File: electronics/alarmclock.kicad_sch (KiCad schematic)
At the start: 31 parts, among them J1 Conn_01x02, J2 SWD, J3 SocketTop, J4 SocketBottom, J5 Conn_01x02, Q1 Backpower, SW1 Rotary_Encoder_Switch, SW2 Reset, U1 STM32L031F6P6, U2 74HC595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

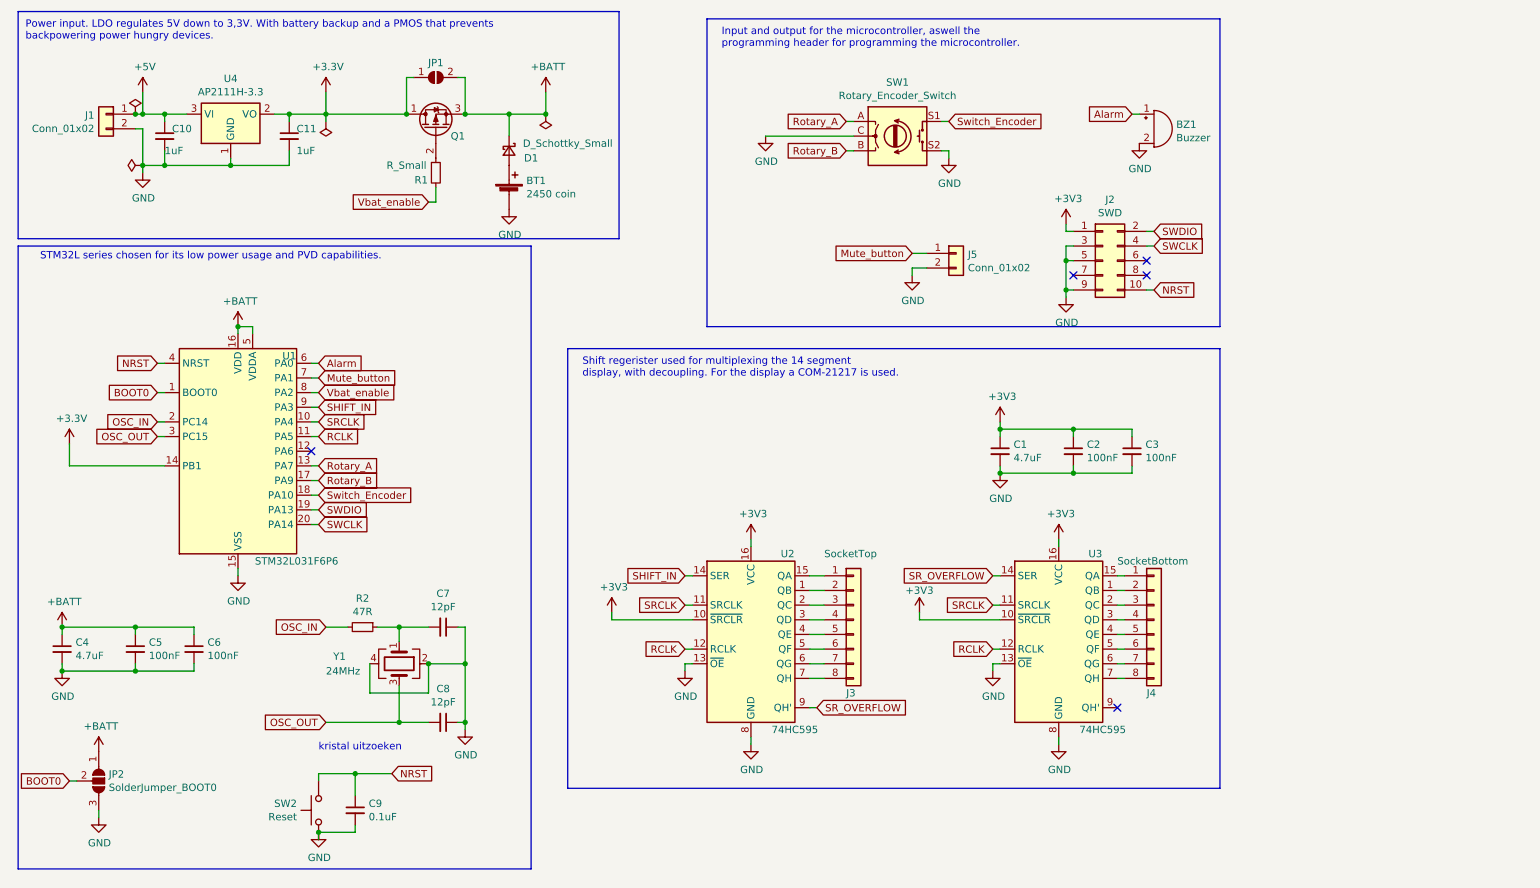
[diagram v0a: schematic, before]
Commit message: added currentlimiting resistors
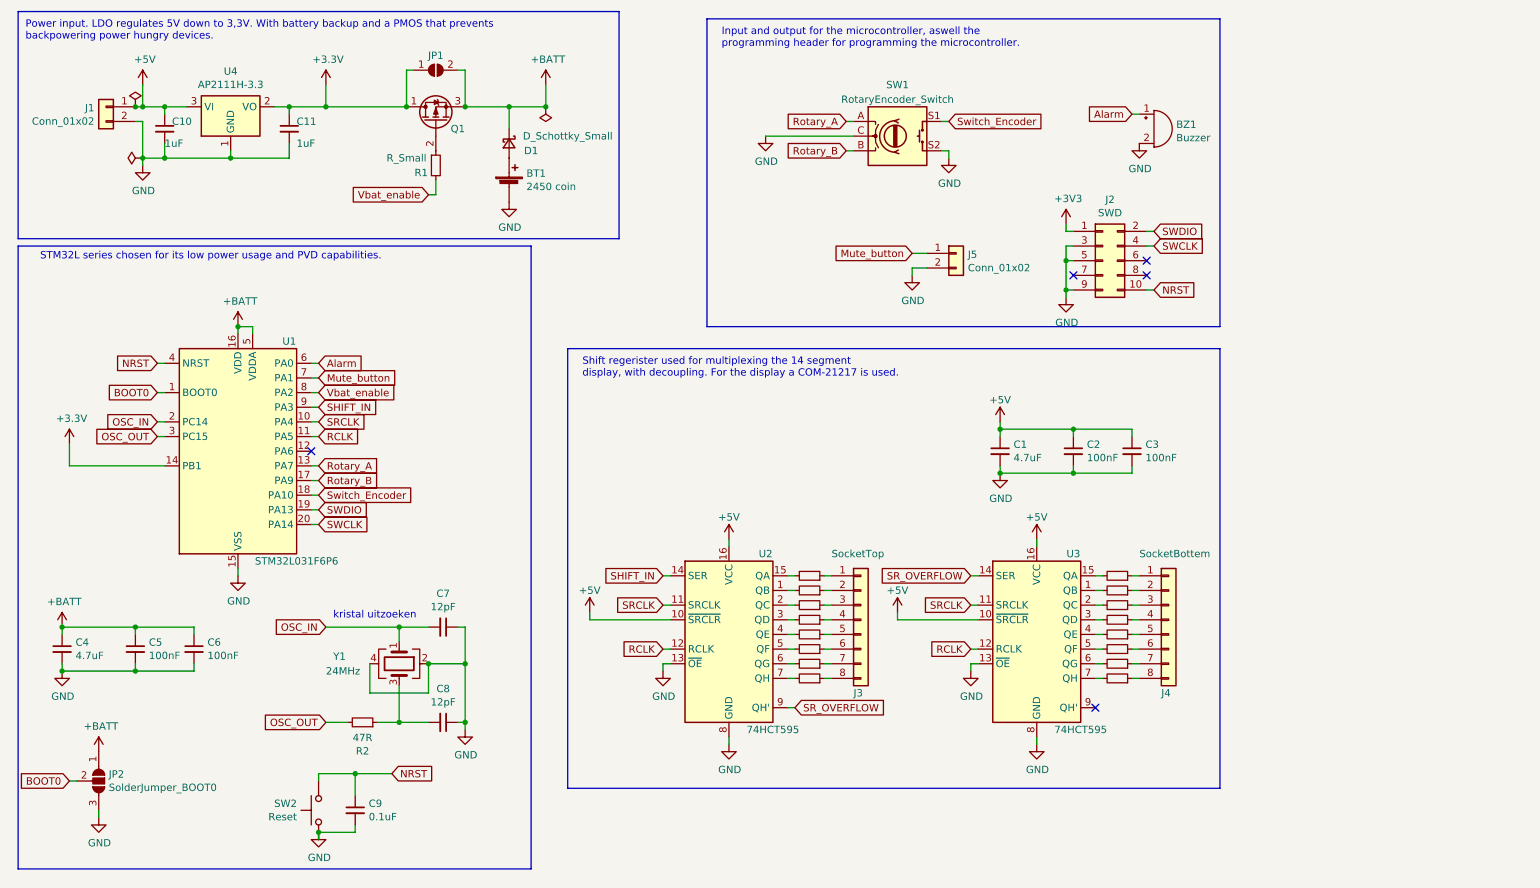
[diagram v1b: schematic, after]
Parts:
- removed SW1: Rotary_Encoder_Switch, Connector_PinHeader_2.54mm:PinHeader_1x05_P2.54mm_Vertical, symbol Device:Rotary_Encoder_Switch
- added R10, R11, R12, R13, R14, R15, R16, R17, R18, R3, R4, R5, R6, R7, R8, R9: R_Small, symbol Device:R_Small
- added SW1: RotaryEncoder_Switch, symbol Device:RotaryEncoder_Switch
- J4: value SocketBottom -> SocketBottem
- U2, U3: value 74HC595 -> 74HCT595
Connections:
- net +3V3: no longer C1.1, C2.1, C3.1, U2.10 (~{SRCLR}), U2.16 (VCC), U3.10 (~{SRCLR}), U3.16 (VCC)
- net +5V: now also C1.1, C2.1, C3.1, U2.10 (~{SRCLR}), U2.16 (VCC), U3.10 (~{SRCLR}), U3.16 (VCC)
- net GND: now also SW1.C, SW1.S2
- net OSC_IN: now also C7.2, Y1.1; no longer R2.2
- net OSC_OUT: now also R2.2; no longer C8.2, Y1.3
- net Rotary_A: now also SW1.A
- net Rotary_B: now also SW1.B
- net Switch_Encoder: now also SW1.S1
- net at U3.15 (QA): now also R9.2; no longer J4.1 (Pin_1)
- net at U3.1 (QB): now also R12.2; no longer J4.2 (Pin_2)
- net at U3.2 (QC): now also R13.2; no longer J4.3 (Pin_3)
- net at U3.3 (QD): now also R14.2; no longer J4.4 (Pin_4)
- net at U3.4 (QE): now also R15.2; no longer J4.5 (Pin_5)
- net at U3.5 (QF): now also R16.2; no longer J4.6 (Pin_6)
- net at U3.6 (QG): now also R17.2; no longer J4.7 (Pin_7)
- net at U3.7 (QH): now also R18.2; no longer J4.8 (Pin_8)
- net at J3.1 (Pin_1): now also R3.1; no longer U2.15 (QA)
- net at J3.2 (Pin_2): now also R4.1; no longer U2.1 (QB)
- net at J3.3 (Pin_3): now also R5.1; no longer U2.2 (QC)
- net at J3.4 (Pin_4): now also R6.1; no longer U2.3 (QD)
- net at J3.5 (Pin_5): now also R7.1; no longer U2.4 (QE)
- net at J3.6 (Pin_6): now also R8.1; no longer U2.5 (QF)
- net at J3.7 (Pin_7): now also R10.1; no longer U2.6 (QG)
- net at J3.8 (Pin_8): now also R11.1; no longer U2.7 (QH)
- new net: C8.2, R2.1, Y1.3
- new net: R4.2, U2.1 (QB)
- new net: R3.2, U2.15 (QA)
- new net: R5.2, U2.2 (QC)
- new net: R6.2, U2.3 (QD)
- new net: R7.2, U2.4 (QE)
- new net: R8.2, U2.5 (QF)
- new net: R10.2, U2.6 (QG)
- new net: R11.2, U2.7 (QH)
- new net: J4.2 (Pin_2), R12.1
- new net: J4.1 (Pin_1), R9.1
- new net: J4.3 (Pin_3), R13.1
- new net: J4.4 (Pin_4), R14.1
- new net: J4.5 (Pin_5), R15.1
- new net: J4.6 (Pin_6), R16.1
- new net: J4.7 (Pin_7), R17.1
- new net: J4.8 (Pin_8), R18.1
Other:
- moved on the sheet: BT1, C10, C11, D1, J1, J3, JP1, Q1, R1, R2, U2, U3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

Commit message: made most of the pcb
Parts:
- removed R13, R14, R15, R16, R5, R6, R7: R_Small, symbol Device:R_Small
- removed R2: 47R, Resistor_SMD:R_1206_3216Metric, symbol Device:R_Small
- added J6, J7: Conn_01x05, Connector_PinHeader_2.54mm:PinHeader_1x05_P2.54mm_Vertical, symbol Connector_Generic:Conn_01x05
- C7, C8: footprint Capacitor_SMD:C_1206_3216Metric -> Capacitor_SMD:C_0805_2012Metric
- D1: footprint (none) -> Diode_SMD:D_1206_3216Metric_Pad1.42x1.75mm_HandSolder
- J1, J5: footprint (none) -> Connector_PinHeader_2.54mm:PinHeader_1x02_P2.54mm_Vertical
- JP1: footprint (none) -> Jumper:SolderJumper-2_P1.3mm_Open_TrianglePad1.0x1.5mm
- JP2: footprint (none) -> Jumper:SolderJumper-3_P2.0mm_Open_TrianglePad1.0x1.5mm
- Q1: footprint (none) -> Package_TO_SOT_SMD:SOT-323_SC-70_Handsoldering
- R1, R10, R11, R12, R17, R18, R3, R4, R8, R9: footprint (none) -> Resistor_SMD:R_1206_3216Metric
- SW1: footprint (none) -> Rotary_Encoder:RotaryEncoder_Bourns_Horizontal_PEC09-2xxxF-Nxxxx
- U2, U3: footprint (none) -> Package_SO:TSSOP-16_4.4x5mm_P0.65mm
- Y1: footprint (none) -> Crystal:Crystal_SMD_SeikoEpson_MC146-4Pin_6.7x1.5mm_HandSoldering
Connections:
- net +5V: now also J1.2 (Pin_2), J6.5 (Pin_5), J7.5 (Pin_5); no longer J1.1 (Pin_1)
- net Alarm: now also BZ1.2 (+); no longer BZ1.1 (-)
- net GND: now also BZ1.1 (-), J1.1 (Pin_1), J5.1 (Pin_1), SW2.1, J6.1 (Pin_1), J7.1 (Pin_1); no longer BZ1.2 (+), J1.2 (Pin_2), J5.2 (Pin_2), SW2.2
- net Mute_button: now also J5.2 (Pin_2); no longer J5.1 (Pin_1)
- net NRST: now also SW2.2; no longer SW2.1
- net OSC_OUT: now also C8.2, Y1.3
- net RCLK: now also U1.9 (PA3), J7.3 (Pin_3); no longer U1.11 (PA5), U2.12 (RCLK), U3.12 (RCLK)
- net Rotary_B: now also U1.11 (PA5); no longer U1.17 (PA9)
- net SHIFT_IN: now also U1.10 (PA4), J7.4 (Pin_4); no longer U1.9 (PA3), U2.14 (SER)
- net SRCLK: now also U1.8 (PA2), J7.2 (Pin_2); no longer U1.10 (PA4), U2.11 (SRCLK), U3.11 (SRCLK)
- net Switch_Encoder: now also U1.12 (PA6); no longer U1.18 (PA10)
- net Vbat_enable: now also U1.17 (PA9); no longer U1.8 (PA2)
- net at J3.3 (Pin_3): now also U2.2 (QC)
- net at J3.4 (Pin_4): now also U2.3 (QD)
- net at J3.5 (Pin_5): now also U2.4 (QE)
- net at U3.2 (QC): now also J4.3 (Pin_3)
- net at U3.3 (QD): now also J4.4 (Pin_4)
- net at U3.4 (QE): now also J4.5 (Pin_5)
- net at U3.5 (QF): now also J4.6 (Pin_6)
- new net RCLK_DIS: J6.3 (Pin_3), U2.12 (RCLK), U3.12 (RCLK)
- new net SHIFT_IN_DIS: J6.4 (Pin_4), U2.14 (SER)
- new net SRCLK_DIS: J6.2 (Pin_2), U2.11 (SRCLK), U3.11 (SRCLK)
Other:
- moved on the sheet: BZ1, C1, C10, C11, C2, C3, J1, J2, J3, J4, J5, SW1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

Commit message: finilised for review
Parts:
- removed SW1: RotaryEncoder_Switch, Rotary_Encoder:RotaryEncoder_Bourns_Horizontal_PEC09-2xxxF-Nxxxx, symbol Device:RotaryEncoder_Switch
- added J8: RotaryEncoder, Connector_PinHeader_2.54mm:PinHeader_1x05_P2.54mm_Vertical, symbol Connector_Generic:Conn_01x05
- BT1: footprint (none) -> Battery:BatteryHolder_ComfortableElectronic_CH273-2450_1x2450
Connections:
- net GND: now also J8.1 (Pin_1), J8.2 (Pin_2)
- net Rotary_A: now also J8.5 (Pin_5)
- net Rotary_B: now also J8.3 (Pin_3)
- net Switch_Encoder: now also J8.4 (Pin_4)
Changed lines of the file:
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@@
   (junction (at 81.28 30.48) (diameter 0) (color 0 0 0 0)
+  )
+  (junction (at 148.59 38.1) (diameter 0) (color 0 0 0 0)
   )
   (junction (at 52.07 68.58) (diameter 0) (color 0 0 0 0)
@@
     (stroke (width 0) (type default))
   )
-  (wire (pts (xy 161.29 36.83) (xy 162.56 36.83))
+  (wire (pts (xy 149.86 38.1) (xy 148.59 38.1))
     (stroke (width 0) (type default))
   )
@@
     (stroke (width 0) (type default))
   )
-  (wire (pts (xy 162.56 31.75) (xy 161.29 31.75))
+  (wire (pts (xy 148.59 35.56) (xy 149.86 35.56))
     (stroke (width 0) (type default))
   )
@@
     (stroke (width 0) (type default))
   )
-  (wire (pts (xy 130.81 34.29) (xy 146.05 34.29))
-    (stroke (width 0) (type default))
-  )
   (wire (pts (xy 189.23 124.46) (xy 187.96 124.46))
     (stroke (width 0) (type default))
@@
     (stroke (width 0) (type default))
   )
-  (wire (pts (xy 144.78 31.75) (xy 146.05 31.75))
+  (wire (pts (xy 148.59 27.94) (xy 149.86 27.94))
     (stroke (width 0) (type default))
   )
@@
     (stroke (width 0) (type default))
   )
-  (wire (pts (xy 162.56 36.83) (xy 162.56 38.1))
+  (wire (pts (xy 148.59 38.1) (xy 148.59 39.37))
     (stroke (width 0) (type default))
   )
@@
     (stroke (width 0) (type default))
   )
+  (wire (pts (xy 148.59 30.48) (xy 149.86 30.48))
+    (stroke (width 0) (type default))
+  )
   (wire (pts (xy 120.65 101.6) (xy 130.81 101.6))
     (stroke (width 0) (type default))
@@
     (stroke (width 0) (type default))
   )
-  (wire (pts (xy 144.78 36.83) (xy 146.05 36.83))
+  (wire (pts (xy 148.59 33.02) (xy 149.86 33.02))
     (stroke (width 0) (type default))
   )
@@
   )
   (wire (pts (xy 219.71 114.3) (xy 220.98 114.3))
+    (stroke (width 0) (type default))
+  )
+  (wire (pts (xy 148.59 35.56) (xy 148.59 38.1))
     (stroke (width 0) (type default))
   )
@@
     )
   )
-  (global_label "Rotary_B" (shape input) (at 144.78 36.83 180)
+  (global_label "Rotary_B" (shape input) (at 148.59 33.02 180)
     (effects (font (size 1.27 1.27)) (justify right))
-    (property "Intersheetrefs" "${INTERSHEET_REFS}" (at 144.78 36.83 0)
-      (effects (font (size 1.27 1.27)) hide)
-    )
-  )
-  (global_label "Switch_Encoder" (shape input) (at 162.56 31.75 0)
-    (effects (font (size 1.27 1.27)) (justify left))
-    (property "Intersheetrefs" "${INTERSHEET_REFS}" (at 162.56 31.75 0)
+    (property "Intersheetrefs" "${INTERSHEET_REFS}" (at 148.59 33.02 0)
+      (effects (font (size 1.27 1.27)) hide)
+    )
+  )
+  (global_label "Switch_Encoder" (shape input) (at 148.59 30.48 180)
+    (effects (font (size 1.27 1.27)) (justify right))
+    (property "Intersheetrefs" "${INTERSHEET_REFS}" (at 148.59 30.48 0)
       (effects (font (size 1.27 1.27)) hide)
     )
@@
     )
   )
-  (global_label "Rotary_A" (shape input) (at 144.78 31.75 180)
+  (global_label "Rotary_A" (shape input) (at 148.59 27.94 180)
     (effects (font (size 1.27 1.27)) (justify right))
-    (property "Intersheetrefs" "${INTERSHEET_REFS}" (at 144.78 31.75 0)
+    (property "Intersheetrefs" "${INTERSHEET_REFS}" (at 148.59 27.94 0)
       (effects (font (size 1.27 1.27)) hide)
     )
@@
     )
   )
-  (symbol (lib_id "power:GND") (at 162.56 38.1 0) (unit 1)
-    (in_bom yes) (on_board yes) (dnp no)
-    (property "Reference" "#PWR07" (at 162.56 44.45 0)
-      (effects (font (size 1.27 1.27)) hide)
-    )
-    (property "Value" "GND" (at 162.687 42.4942 0)
-      (effects (font (size 1.27 1.27)))
-    )
-    (property "Footprint" "" (at 162.56 38.1 0)
-      (effects (font (size 1.27 1.27)) hide)
-    )
-    (property "Datasheet" "" (at 162.56 38.1 0)
+  (symbol (lib_id "power:GND") (at 148.59 39.37 0) (mirror y) (unit 1)
+    (in_bom yes) (on_board yes) (dnp no)
+    (property "Reference" "#PWR07" (at 148.59 45.72 0)
+      (effects (font (size 1.27 1.27)) hide)
+    )
+    (property "Value" "GND" (at 148.463 43.7642 0)
+      (effects (font (size 1.27 1.27)))
+    )
+    (property "Footprint" "" (at 148.59 39.37 0)
+      (effects (font (size 1.27 1.27)) hide)
+    )
+    (property "Datasheet" "" (at 148.59 39.37 0)
       (effects (font (size 1.27 1.27)) hide)
     )
@@
       (effects (font (size 1.27 1.27)) (justify left))
     )
-    (property "Footprint" "" (at 99.06 42.926 90)
+    (property "Footprint" "Battery:BatteryHolder_ComfortableElectronic_CH273-2450_1x2450" (at 99.06 42.926 90)
       (effects (font (size 1.27 1.27)) hide)
     )
@@
         (path "/fcd099cf-d7c6-418d-b6d0-a7fbd5aabc64"
           (reference "R1") (unit 1)
-        )
-      )
-    )
-  )
-  (symbol (lib_id "power:GND") (at 130.81 34.29 0) (unit 1)
-    (in_bom yes) (on_board yes) (dnp no)
-    (property "Reference" "#PWR0106" (at 130.81 40.64 0)
-      (effects (font (size 1.27 1.27)) hide)
-    )
-    (property "Value" "GND" (at 130.937 38.6842 0)
-      (effects (font (size 1.27 1.27)))
-    )
-    (property "Footprint" "" (at 130.81 34.29 0)
-      (effects (font (size 1.27 1.27)) hide)
-    )
-    (property "Datasheet" "" (at 130.81 34.29 0)
-      (effects (font (size 1.27 1.27)) hide)
-    )
-    (pin "1")
-    (instances
-      (project "alarmclock"
-        (path "/fcd099cf-d7c6-418d-b6d0-a7fbd5aabc64"
-          (reference "#PWR0106") (unit 1)
         )
       )
@@
     )
   )
-  (symbol (lib_id "Device:RotaryEncoder_Switch") (at 153.67 34.29 0) (unit 1)
-    (in_bom yes) (on_board yes) (dnp no) (fields_autoplaced)
-    (property "Reference" "SW1" (at 153.67 25.4 0)
-      (effects (font (size 1.27 1.27)))
-    )
-    (property "Value" "RotaryEncoder_Switch" (at 153.67 27.94 0)
-      (effects (font (size 1.27 1.27)))
-    )
-    (property "Footprint" "Rotary_Encoder:RotaryEncoder_Bourns_Horizontal_PEC09-2xxxF-Nxxxx" (at 149.86 30.226 0)
-      (effects (font (size 1.27 1.27)) hide)
-    )
-    (property "Datasheet" "~" (at 153.67 27.686 0)
-      (effects (font (size 1.27 1.27)) hide)
-    )
-    (pin "A")
-    (pin "B")
-    (pin "C")
-    (pin "S1")
-    (pin "S2")
-    (instances
-      (project "alarmclock"
-        (path "/fcd099cf-d7c6-418d-b6d0-a7fbd5aabc64"
-          (reference "SW1") (unit 1)
-        )
-      )
-    )
-  )
   (symbol (lib_id "Device:R_Small") (at 191.77 114.3 270) (mirror x) (unit 1)
     (in_bom yes) (on_board yes) (dnp no)
@@
         )
       )
+    )
+  )
+  (symbol (lib_id "Connector_Generic:Conn_01x05") (at 154.94 33.02 0) (mirror x) (unit 1)
+    (in_bom yes) (on_board yes) (dnp no)
+    (property "Reference" "J8" (at 154.94 22.86 0)
+      (effects (font (size 1.27 1.27)))
+    )
+    (property "Value" "RotaryEncoder" (at 154.94 25.4 0)
+      (effects (font (size 1.27 1.27)))
+    )
+    (property "Footprint" "Connector_PinHeader_2.54mm:PinHeader_1x05_P2.54mm_Vertical" (at 154.94 33.02 0)
+      (effects (font (size 1.27 1.27)) hide)
+    )
+    (property "Datasheet" "~" (at 154.94 33.02 0)
+      (effects (font (size 1.27 1.27)) hide)
+    )
+    (pin "1")
+    (pin "2")
+    (pin "3")
+    (pin "4")
+    (pin "5")
+    (instances
+      (project "alarmclock"
+        (path "/fcd099cf-d7c6-418d-b6d0-a7fbd5aabc64"
+          (reference "J8") (unit 1)
+        )
+      )
